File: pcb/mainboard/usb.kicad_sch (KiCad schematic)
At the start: 73 parts

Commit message: - Upgrade KiCad to latest version - Working on PM circuits - Initial USB Type-C support - Initial support for LCD
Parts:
- removed C? (x2): 18pF, Capacitor_SMD:C_0603_1608Metric, symbol Device:C
- removed C? (x4): 100nF, Capacitor_SMD:C_0603_1608Metric, symbol Device:C
- removed C?: 1uF, symbol Device:C
- removed C? (x17): 10nF, symbol Device:C
- removed C? (x9): 100nF, symbol Device:C
- removed C? (x3): 10uF/6.3V, symbol Device:C
- removed D?: RCLAMP3346P, footprints:UDFN-7_0.8x2.7mm_P0.4mm, symbol symbols:RCLAMP3346P
- removed FB?: BLM21PG600SN1, symbol Device:Ferrite_Bead
- removed FL? (x3): DLP11SN161SL2, footprints:Filter_125100, symbol Device:EMI_Filter_LL_1423
- removed J?: USB3_A, footprints:USB3_A_1.36_SINK, symbol Connector:USB3_A
- removed R? (x3): 0, Resistor_SMD:R_0603_1608Metric, symbol Device:R
- removed R?: 1.6K/1%, Resistor_SMD:R_0603_1608Metric, symbol Device:R
- removed R?: 10K, symbol Device:R
- removed R? (x2): 10K, Resistor_SMD:R_0603_1608Metric, symbol Device:R
- removed U?: uPD720201, Package_DFN_QFN:QFN-68-1EP_8x8mm_P0.4mm_EP5.2x5.2mm_ThermalVias, symbol symbols:uPD720201
- removed U?: 25LCxxx, symbol Memory_EEPROM:25LCxxx
- removed Y?: 25MHz, Crystal:Crystal_SMD_3225-4Pin_3.2x2.5mm, symbol Device:Crystal_GND24
- added C? (x11): 100nF, Capacitor_SMD:C_0201_0603Metric, symbol Device:C
- added C?: 10uF, Capacitor_SMD:C_0402_1005Metric, symbol Device:C
- added J?: USB_C_Receptacle, Connector_USB:USB_C_Receptacle_Amphenol_12401548E4-2A, symbol Connector:USB_C_Receptacle
- added L?: EXC14CE900U, footprint:L_CommonModeChoke_Panasonic_EXC14CE, symbol Device:L_Coupled_Small_1423
- added L?: 300R, Inductor_SMD:L_0603_1608Metric, symbol Device:L
- added U?: USBLC6-2P6, Package_TO_SOT_SMD:SOT-666, symbol Power_Protection:USBLC6-2P6
- added U?: CBTL08GP053, footprint:BGA-40_6x9_3.5x5.0mm, symbol symbols:CBTL08GP053
- added U?: FUSB302BMPX, Package_DFN_QFN:WQFN-14-1EP_2.5x2.5mm_P0.5mm_EP1.45x1.45mm, symbol Interface_USB:FUSB302BMPX
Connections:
- net +3V3: now also C?.1, C?.1, C?.1, U?.12 (VCONN), U?.13 (VCONN), U?.3 (VDD), U?.4 (VDD), U?.B2 (VDD), U?.E3 (VDD), U?.E4 (VDDIO), U?.H3 (VDDIO), U?.J5 (SW_EN)
- net GND: now also C?.2, C?.2, C?.2, C?.2, J?.A1 (GND), J?.A12 (GND), J?.B1 (GND), J?.B12 (GND), J?.S1 (SHIELD), U?.15 (GND), U?.2 (GND), U?.8 (GND), U?.9 (GND), U?.B3 (IP8A), U?.B4 (IP8B), U?.B5 (GND), U?.D3 (GND), U?.D4 (SLV_ADDR2), U?.F3 (GND), U?.F4 (GND), U?.H2 (GND), U?.H5 (SLV_ADDR1)
- new net: C?.2, U?.A1 (IP6+)
- new net: C?.2, U?.B1 (IP5-)
- new net: C?.2, U?.A2 (IP6-)
- new net: C?.2, U?.A4 (IP7B)
- new net: C?.2, U?.C1 (IP5+)
- new net: J?.A5 (CC1), U?.10 (CC1), U?.11 (CC1)
- new net: J?.B5 (CC2), U?.1 (CC2), U?.14 (CC2)
- new net: C?.2, U?.A3 (IP7A)
- new net: C?.2, U?.D1 (IP4-)
- new net: C?.2, U?.E1 (IP4+)
- new net DP_AUXN: C?.1
- new net DP_AUXP: C?.1
- new net DP_N0: U?.G1 (IP3-)
- new net DP_N1: C?.1
- new net DP_N2: C?.1
- new net DP_N3: U?.J1 (IP2-)
- new net DP_P0: U?.F1 (IP3+)
- new net DP_P1: C?.1
- new net DP_P2: C?.1
- new net DP_P3: U?.H1 (IP2+)
- new net I2C3_SCL: U?.6 (SCL), U?.H4 (I2C_SDA)
- new net I2C3_SDA: U?.7 (SDA), U?.J4 (I2C_CLK)
- new net TYPEC_DN: J?.A7 (D-), J?.B7 (D-), L?.4, U?.3 (I/O2), U?.4 (I/O2)
- new net TYPEC_DP: J?.A6 (D+), J?.B6 (D+), L?.3, U?.1 (I/O1), U?.6 (I/O1)
- new net TYPEC_RX1N: J?.B10 (RX1-), U?.J6 (OP1-)
- new net TYPEC_RX1P: J?.B11 (RX1+), U?.H6 (OP1+)
- new net TYPEC_RX2N: J?.A10 (RX2-), U?.E6 (OP2-)
- new net TYPEC_RX2P: J?.A11 (RX2+), U?.D6 (OP2+)
- new net TYPEC_SBU1: J?.A8 (SBU1), U?.A5 (OP5A)
- new net TYPEC_SBU2: J?.B8 (SBU2), U?.A6 (OP5B)
- new net TYPEC_TX1N: J?.A3 (TX1-), U?.F6 (OP3-)
- new net TYPEC_TX1P: J?.A2 (TX1+), U?.G6 (OP3+)
- new net TYPEC_TX2N: J?.B3 (TX2-), U?.B6 (OP4-)
- new net TYPEC_TX2P: J?.B2 (TX2+), U?.C6 (OP4+)
- new net USB3_SSRXN: U?.J3 (IP1-)
- new net USB3_SSRXP: U?.J2 (IP1+)
- new net USB3_SSTXN: C?.1
- new net USB3_SSTXP: C?.1
- new net USB_DM: L?.1
- new net USB_DP: L?.2
- new net VBUS: C?.1, L?.1
- new net VBUS_IN: J?.A4 (VBUS), J?.A9 (VBUS), J?.B4 (VBUS), J?.B9 (VBUS), L?.2, U?.2 (VBUS), U?.5 (VBUS)
- no-connect marks 26 -> 10
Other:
- note added: "Switch can be turned off by I2C"
- note removed: "Currently IO sub-board only supports USB 2.0 We expect to use USB 3.0 in the future revisions"
- moved on the sheet: C?, R?, U?, Y?

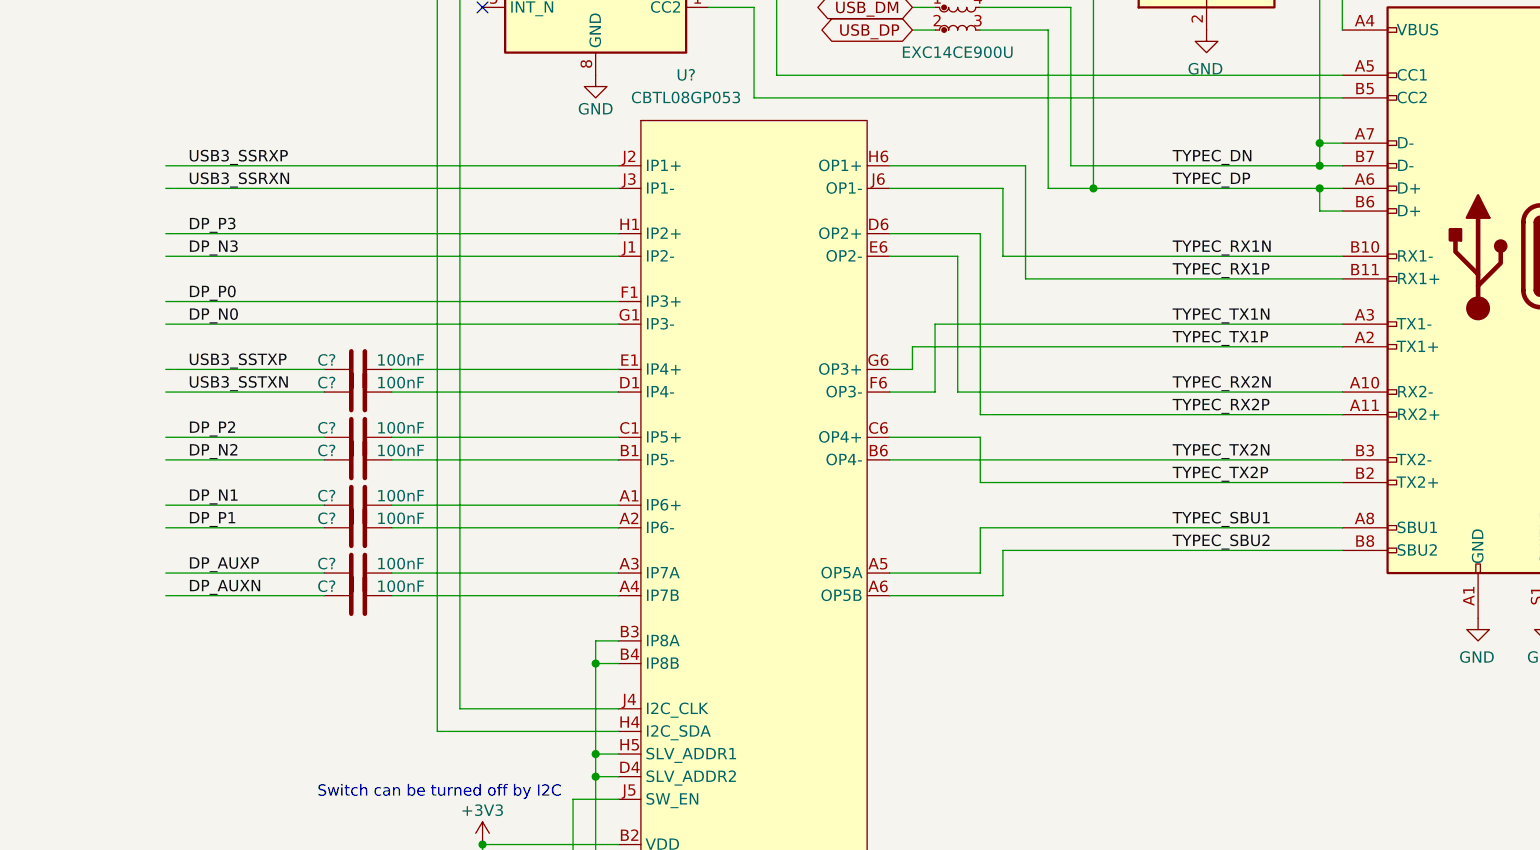
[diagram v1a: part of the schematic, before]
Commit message: - pcb: switch to imx7 for the prototype
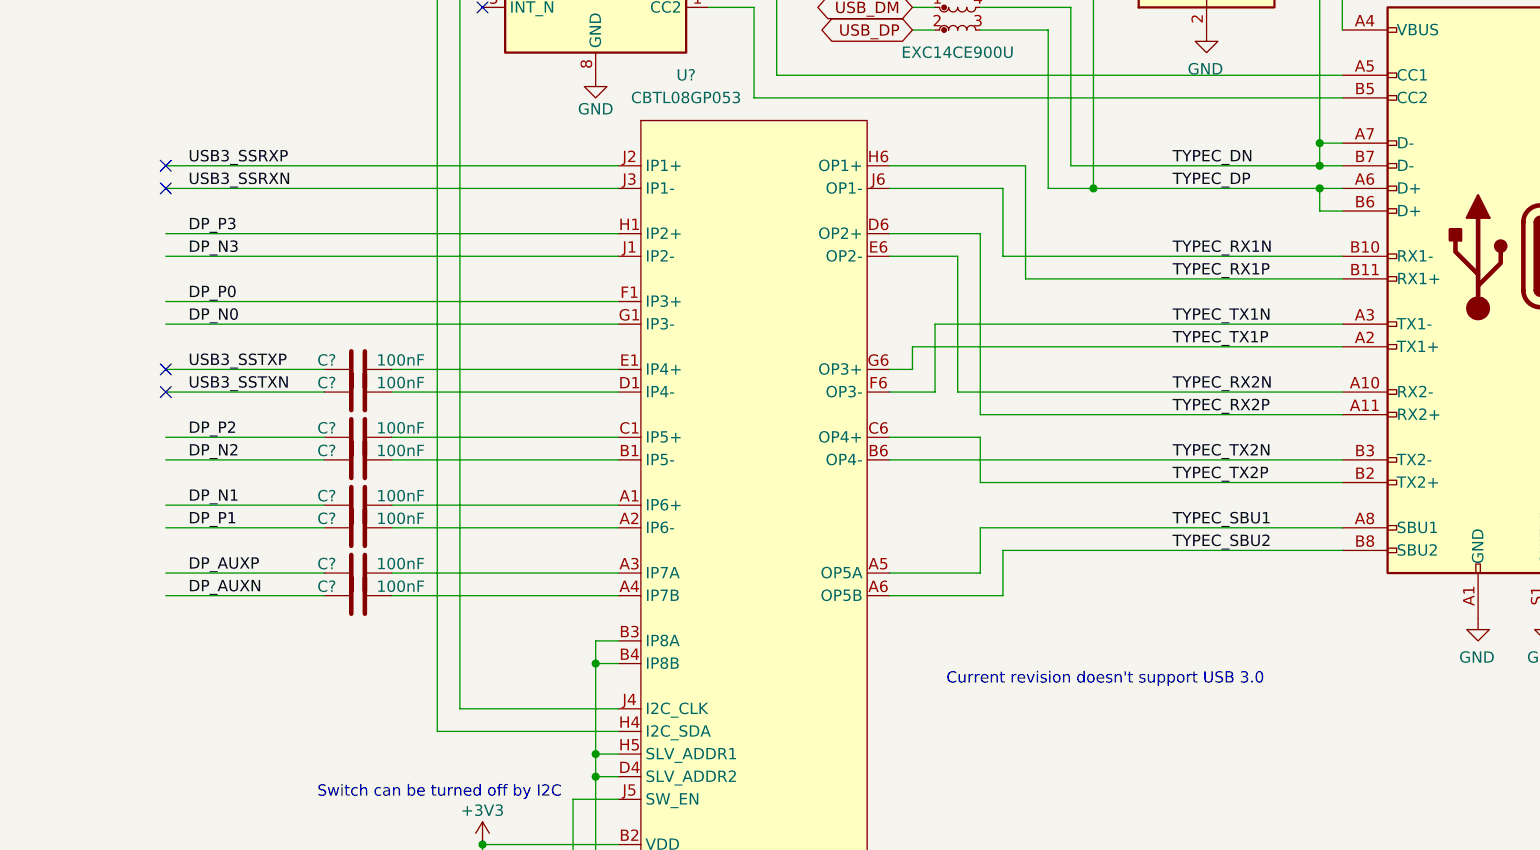
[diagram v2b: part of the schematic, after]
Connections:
- no-connect marks 10 -> 14
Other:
- note added: "Current revision doesn't support USB 3.0"
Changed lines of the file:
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@@
   (no_connect (at 139.065 144.78))
   (no_connect (at 139.065 147.32))
+  (no_connect (at 204.47 107.95))
+  (no_connect (at 204.47 110.49))
+  (no_connect (at 204.47 130.81))
+  (no_connect (at 204.47 133.35))
   (no_connect (at 240.03 90.17))
   (wire (pts (xy 52.705 127) (xy 52.705 134.62))
@@
     (effects (font (size 1.27 1.27)) (justify right bottom))
   )
+  (text "Current revision doesn't support USB 3.0" (at 292.1 166.37 0)
+    (effects (font (size 1.27 1.27)) (justify left bottom))
+  )
   (label "PPON4" (at 93.345 186.69 0)

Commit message: - pcb: working on r0p1 sch
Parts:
- removed C? (x10): 100nF, Capacitor_SMD:C_0201_0603Metric, symbol Device:C
- removed J?: USB_C_Receptacle, Connector_USB:USB_C_Receptacle_Amphenol_12401548E4-2A, symbol Connector:USB_C_Receptacle
- removed U?: CBTL08GP053, footprint:BGA-40_6x9_3.5x5.0mm, symbol symbols:CBTL08GP053
- added J? (x2): USB_A, Connector_USB:USB_A_Molex_67643_Horizontal, symbol Connector:USB_A
- added J?: USB_C_Receptacle_USB2.0, Connector_USB:USB_C_Receptacle_HRO_TYPE-C-31-M-12, symbol Connector:USB_C_Receptacle_USB2.0
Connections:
- net OCI3B is gone; now on net OCI2B: U?.3 (~FLG)
- net OCI4B is gone; now on net OCI1B: U?.3 (~FLG)
- net PPON3 is gone; now on net PPON2: U?.4 (EN)
- net PPON4 is gone; now on net PPON1: U?.4 (EN)
- net GND: now also J?.4 (GND), J?.4 (GND), J?.5 (Shield), J?.5 (Shield), J?.A1 (GND), J?.A12 (GND), J?.B1 (GND), J?.B12 (GND), J?.S1 (SHIELD)
- net TYPEC_DN: now also J?.A7 (D-), J?.B7 (D-)
- net TYPEC_DP: now also J?.A6 (D+), J?.B6 (D+)
- net VBUS_IN: now also J?.A4 (VBUS), J?.A9 (VBUS), J?.B4 (VBUS), J?.B9 (VBUS)
- net PPON1: now reaches U?.12 (PRTPWR1/BC_EN1)
- net OCI1B: now reaches U?.13 (OCS_N1)
- net PPON2: now reaches U?.16 (PRTPWR2/BC_EN2)
- net OCI2B: now reaches U?.17 (OCS_N2)
- net USB_HOST_DN: now reaches U?.30 (USBDM_UP)
- net USB_HOST_DP: now reaches U?.31 (USBDP_UP)
- net at U?.10 (CC1), U?.11 (CC1): now also J?.A5 (CC1)
- net at U?.1 (CC2), U?.14 (CC2): now also J?.B5 (CC2)
- net BT_USB_DM renamed USB_DM2
- net USB_DM2: now also J?.2 (D-)
- net BT_USB_DP renamed USB_DP2
- net USB_DP2: now also J?.3 (D+)
- net CAM_USB_DM renamed EC_USB_DM
- net CAM_USB_DP renamed EC_USB_DP
- net CARD_USB_DM: no longer names the net of U?.8 (USBDM_DN4/PRT_DIS_M4)
- net CARD_USB_DP: no longer names the net of U?.9 (USBDP_DN4/PRT_DIS_P4)
- net I2C3_SCL renamed EC_I2C_SCL
- net I2C3_SDA renamed EC_I2C_SDA
- net KBD_USB_DM renamed USB_DM1
- net USB_DM1: now also J?.2 (D-)
- net KBD_USB_DP renamed USB_DP1
- net USB_DP1: now also J?.3 (D+)
- net VBUS_CH0 renamed VBUS1
- net VBUS1: now also J?.1 (VBUS)
- net VBUS_CH12 renamed VBUS2
- net VBUS2: now also J?.1 (VBUS)
- no-connect marks 14 -> 10
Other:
- note removed: "Current revision doesn't support USB 3.0"
- note removed: "Switch can be turned off by I2C"
- moved on the sheet: C?, R?, U?, Y?

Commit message: - pcb: r0p1 sch draft
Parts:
- gave numbers to parts that had none: 30
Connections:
- net +3V3: no longer C613.1, U604.12 (VCONN), U604.13 (VCONN), U604.3 (VDD), U604.4 (VDD)
- new net +3V3_SB: C613.1, U604.12 (VCONN), U604.13 (VCONN), U604.3 (VDD), U604.4 (VDD)

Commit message: - pcb: start r0p1 layout
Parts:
- added C615, C616: 100nF, Capacitor_SMD:C_0402_1005Metric, symbol Device:C
- added C617, C618: 10uF/6.3V, Capacitor_SMD:C_0603_1608Metric, symbol Device:C
- added D601, D602: LED, LED_SMD:LED_0603_1608Metric, symbol Device:LED
- added J604: USB_B_Micro, Connector_USB:USB_Micro-B_Amphenol_10103594-0001LF_Horizontal, symbol Connector:USB_B_Micro
- added R606, R607: 1K, Resistor_SMD:R_0402_1005Metric, symbol Device:R
- added R608: 100K, Resistor_SMD:R_0402_1005Metric, symbol Device:R
- added R609: 10K, Resistor_SMD:R_0402_1005Metric, symbol Device:R
- added R610: 20K, Resistor_SMD:R_0402_1005Metric, symbol Device:R
- added U606: CP2102N-Axx-xQFN28, Package_DFN_QFN:QFN-28-1EP_5x5mm_P0.5mm_EP3.35x3.35mm, symbol Interface_USB:CP2102N-Axx-xQFN28
- C602: value 0.1uF -> 100nF; footprint (none) -> Capacitor_SMD:C_0402_1005Metric
- C604, C607, C608, C609, C610, C611: footprint (none) -> Capacitor_SMD:C_0402_1005Metric
- C612: footprint (none) -> Capacitor_SMD:C_0603_1608Metric
- C613: footprint Capacitor_SMD:C_0201_0603Metric -> Capacitor_SMD:C_0402_1005Metric
- C614: value 10uF -> 10uF/25V; footprint Capacitor_SMD:C_0402_1005Metric -> Capacitor_SMD:C_0805_2012Metric
- J601, J602: footprint Connector_USB:USB_A_Molex_67643_Horizontal -> footprints:Connector_USB_905-562A2021S10100
- L601: footprint footprint:L_CommonModeChoke_Panasonic_EXC14CE -> footprints:L_CommonModeChoke_Panasonic_EXC14CE
- L602: value 300R -> 120R
- R601: footprint (none) -> Resistor_SMD:R_0402_1005Metric
- R602, R603, R604, R605: footprint Resistor_SMD:R_0603_1608Metric -> Resistor_SMD:R_0402_1005Metric
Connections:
- net GND: now also C615.2, C616.2, C617.2, C618.2, J604.4 (ID), J604.5 (GND), J604.6 (Shield), R610.2, U606.29 (GND), U606.3 (GND)
- net USB_DM renamed USB_OTG_DN
- net USB_DP renamed USB_OTG_DP
- new net: D601.2 (A), R606.1
- new net: C615.1, C617.1, R606.2, R607.2, R608.1, U606.6 (VDD)
- new net: D601.1 (K), U606.18 (~RXT~/GPIO.1)
- new net: D602.1 (K), U606.19 (~TXT~/GPIO.0)
- new net: J604.3 (D+), U606.4 (D+)
- new net: J604.2 (D-), U606.5 (D-)
- new net: C616.1, C618.1, J604.1 (VBUS), R609.1, U606.7 (VREGIN)
- new net: R609.2, R610.1, U606.8 (VBUS)
- new net: R608.2, U606.9 (~RST)
- new net: D602.2 (A), R607.1
- new net UART1_RXD: U606.26 (TXD)
- new net UART1_TXD: U606.25 (RXD)
- no-connect marks 10 -> 26
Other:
- company: Copyright EI-2030 2021. -> Copyright EI-2030 2021. / Engineer: Wenting Zhang
- title: Archer -> Archer Mainboard
- moved on the sheet: L601

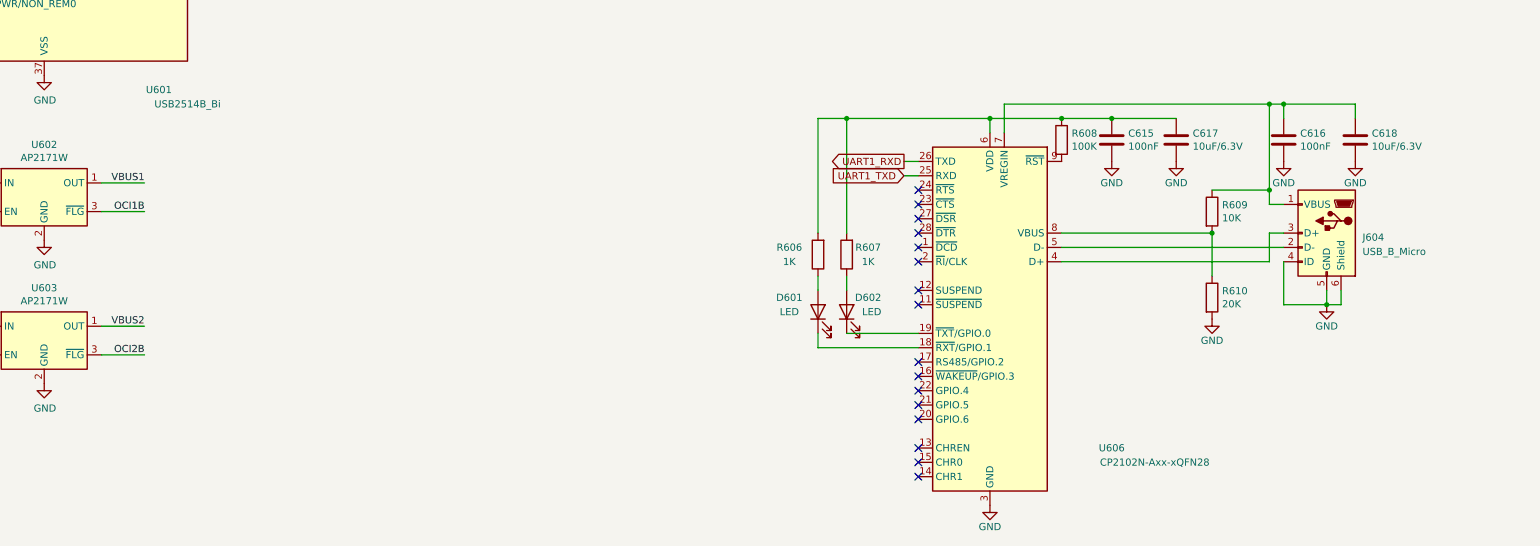
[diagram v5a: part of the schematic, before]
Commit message: - pcb: components placed
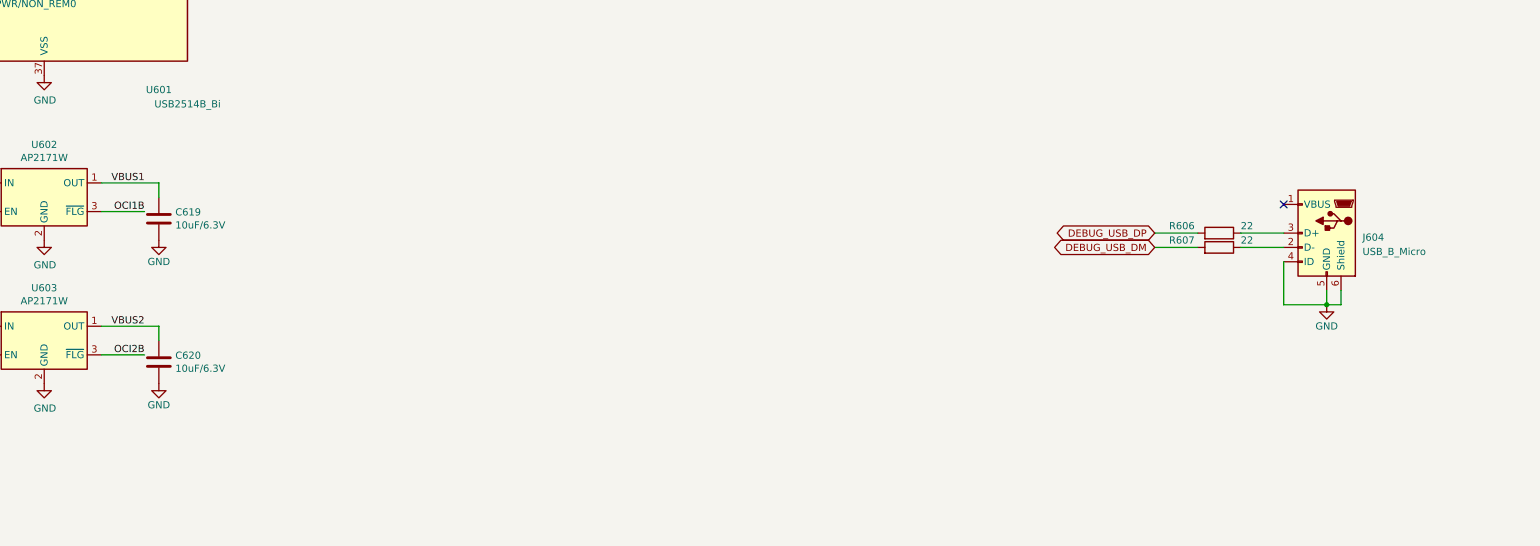
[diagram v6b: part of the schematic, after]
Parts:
- removed C615, C616: 100nF, Capacitor_SMD:C_0402_1005Metric, symbol Device:C
- removed C617, C618: 10uF/6.3V, Capacitor_SMD:C_0603_1608Metric, symbol Device:C
- removed D601, D602: LED, LED_SMD:LED_0603_1608Metric, symbol Device:LED
- removed R608: 100K, Resistor_SMD:R_0402_1005Metric, symbol Device:R
- removed R609: 10K, Resistor_SMD:R_0402_1005Metric, symbol Device:R
- removed R610: 20K, Resistor_SMD:R_0402_1005Metric, symbol Device:R
- removed U606: CP2102N-Axx-xQFN28, Package_DFN_QFN:QFN-28-1EP_5x5mm_P0.5mm_EP3.35x3.35mm, symbol Interface_USB:CP2102N-Axx-xQFN28
- added C619, C620: 10uF/6.3V, Capacitor_SMD:C_0603_1608Metric, symbol Device:C
- C601, C603, C605, C606: footprint Capacitor_SMD:C_0603_1608Metric -> Capacitor_SMD:C_0402_1005Metric
- R606, R607: value 1K -> 22
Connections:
- net GND: now also C619.2, C620.2
- net VBUS1: now also C619.1
- net VBUS2: now also C620.1
- net at R606.1: now also J604.3 (D+)
- net DEBUG_USB_DM: now reaches R607.2
- net DEBUG_USB_DM: no longer R606.2
- net at J604.2 (D-): now also R607.1
- new net DEBUG_USB_DP: R606.2
- no-connect marks 26 -> 11

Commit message: - pcb: finishing layout r0p1
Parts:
- added C615: 100nF, Capacitor_SMD:C_0402_1005Metric, symbol Device:C
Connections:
- net +3V3_SB: now also C615.1
- net GND: now also C615.2
- net OCI1B: now also U601.19 (OCS_N3); no longer U601.13 (OCS_N1)
- net PPON1: now also U601.18 (PRTPWR3/BC_EN3); no longer U601.12 (PRTPWR1/BC_EN1)
- net DEBUG_USB_DM renamed DEBUG_USB_D-
- net DEBUG_USB_DP renamed DEBUG_USB_D+
- net EC_USB_DM renamed USB_D1-
- net USB_D1-: now also J601.2 (D-)
- net EC_USB_DP renamed USB_D1+
- net USB_D1+: now also J601.3 (D+)
- net USB_DM1 renamed EC_USB_D-
- net EC_USB_D-: no longer J601.2 (D-)
- net USB_DM2 renamed USB_D2-
- net USB_DP1 renamed EC_USB_D+
- net EC_USB_D+: no longer J601.3 (D+)
- net USB_DP2 renamed USB_D2+
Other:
- moved on the sheet: C613, J601, J602
